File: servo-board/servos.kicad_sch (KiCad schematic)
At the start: 14 parts, among them M1 Motor_Servo, M2 Motor_Servo, M3 Motor_Servo, M4 Motor_Servo, M5 Motor_Servo, M6 Motor_Servo, M7 Motor_Servo, M8 Motor_Servo, U3 ADUM1401CRWZ, U4 ADUM1401CRWZ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

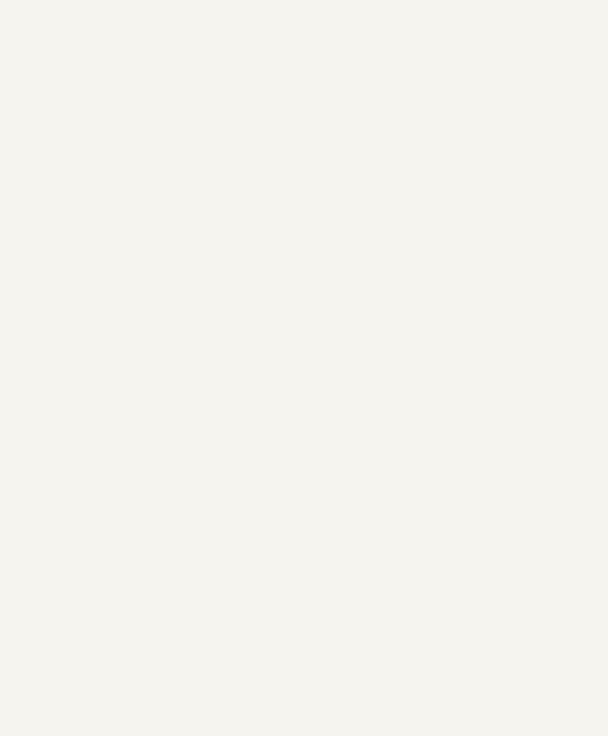
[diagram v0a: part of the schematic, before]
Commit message: control board ordered
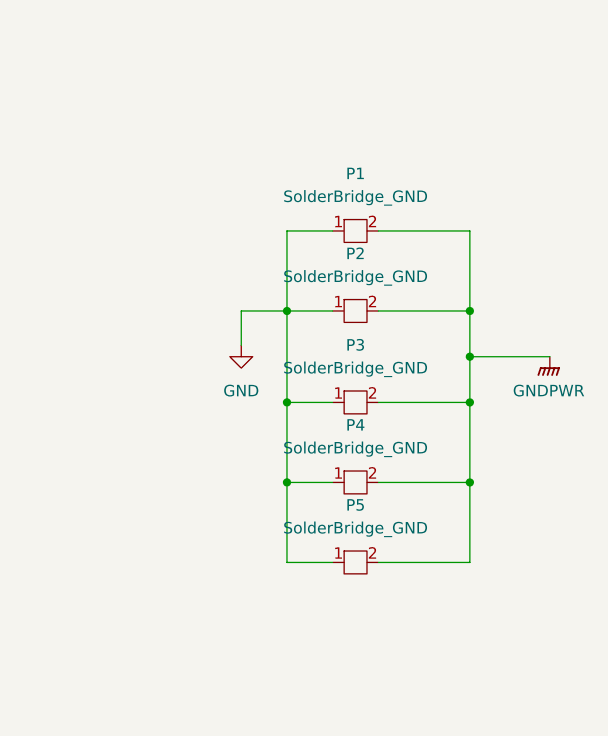
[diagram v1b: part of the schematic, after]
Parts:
- added P1, P2, P3, P4, P5: SolderBridge_GND, bio-robot:SolderBridge_GND, symbol bio-robot:SolderBridge_GND
- M1, M2, M3, M4, M5, M6, M7, M8: footprint bio-robot:PinSocket_1x03_P2.54mm_Vertical -> bio-robot:PinHeader_1x03_P2.54mm_Vertical
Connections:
- net GND: now also P1.1, P2.1, P3.1, P4.1, P5.1
- net GNDPWR: now also P1.2, P2.2, P3.2, P4.2, P5.2

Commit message: changes
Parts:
- U3, U4: value ADUM1401CRWZ -> ADUM1400CRWZ; symbol bio-robot:ADUM1401CRWZ -> bio-robot:ADUM1400CRWZ
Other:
- note added: "Digital Isolators (for PWM Signals)"
- note added: "Ground Bridge (if non-isolated)"
- note added: "Servo 5V Logic Level Adjustment (For secondary side of isolators)"
- note added: "Servo Headers"
- moved on the sheet: C1, C2, M1, M2, M3, M4, M5, M6, M7, M8, P1, P2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
